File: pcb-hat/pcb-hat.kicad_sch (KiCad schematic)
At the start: 64 parts, among them Q1 NTMFS5C468NLT1G, Q2 Q_NPN, Q3 Q_PMOS_GSD, U1 AOZ6605PI-1, U2 INA219AxD, U3 INA219AxD, U4 HTD Servo, U5 Power_Connector, U6 AOZ6605PI-1, U7 Raspberry_Pi_Generic

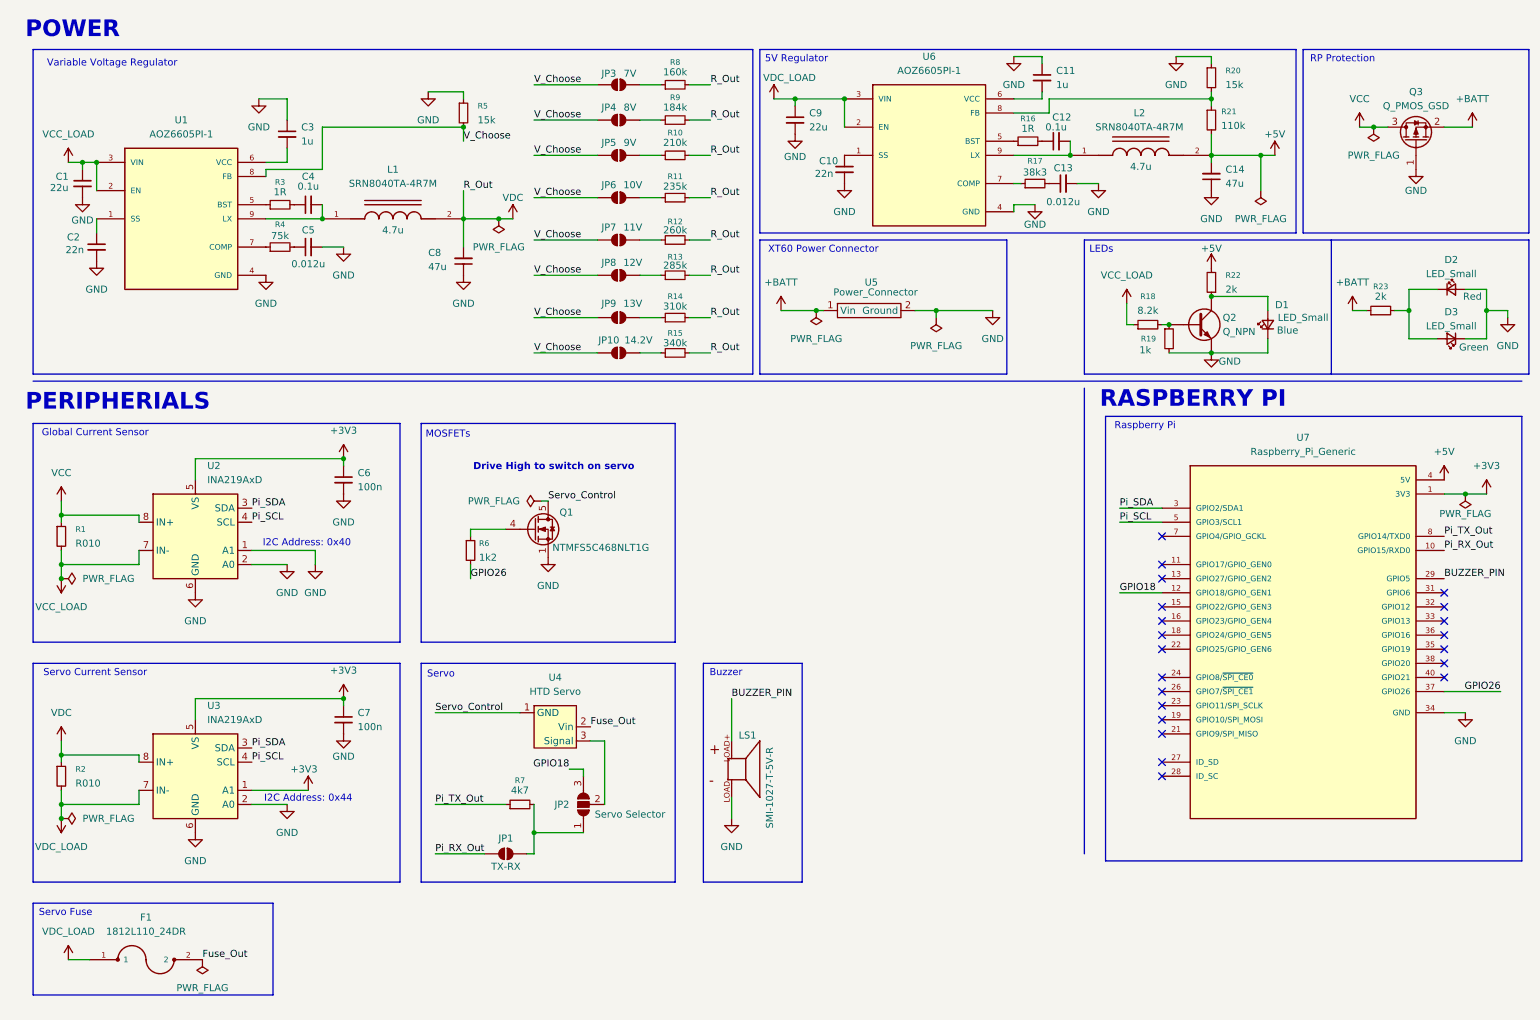
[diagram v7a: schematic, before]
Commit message: Update schematic and reroute PCB
See the github PR for all changes
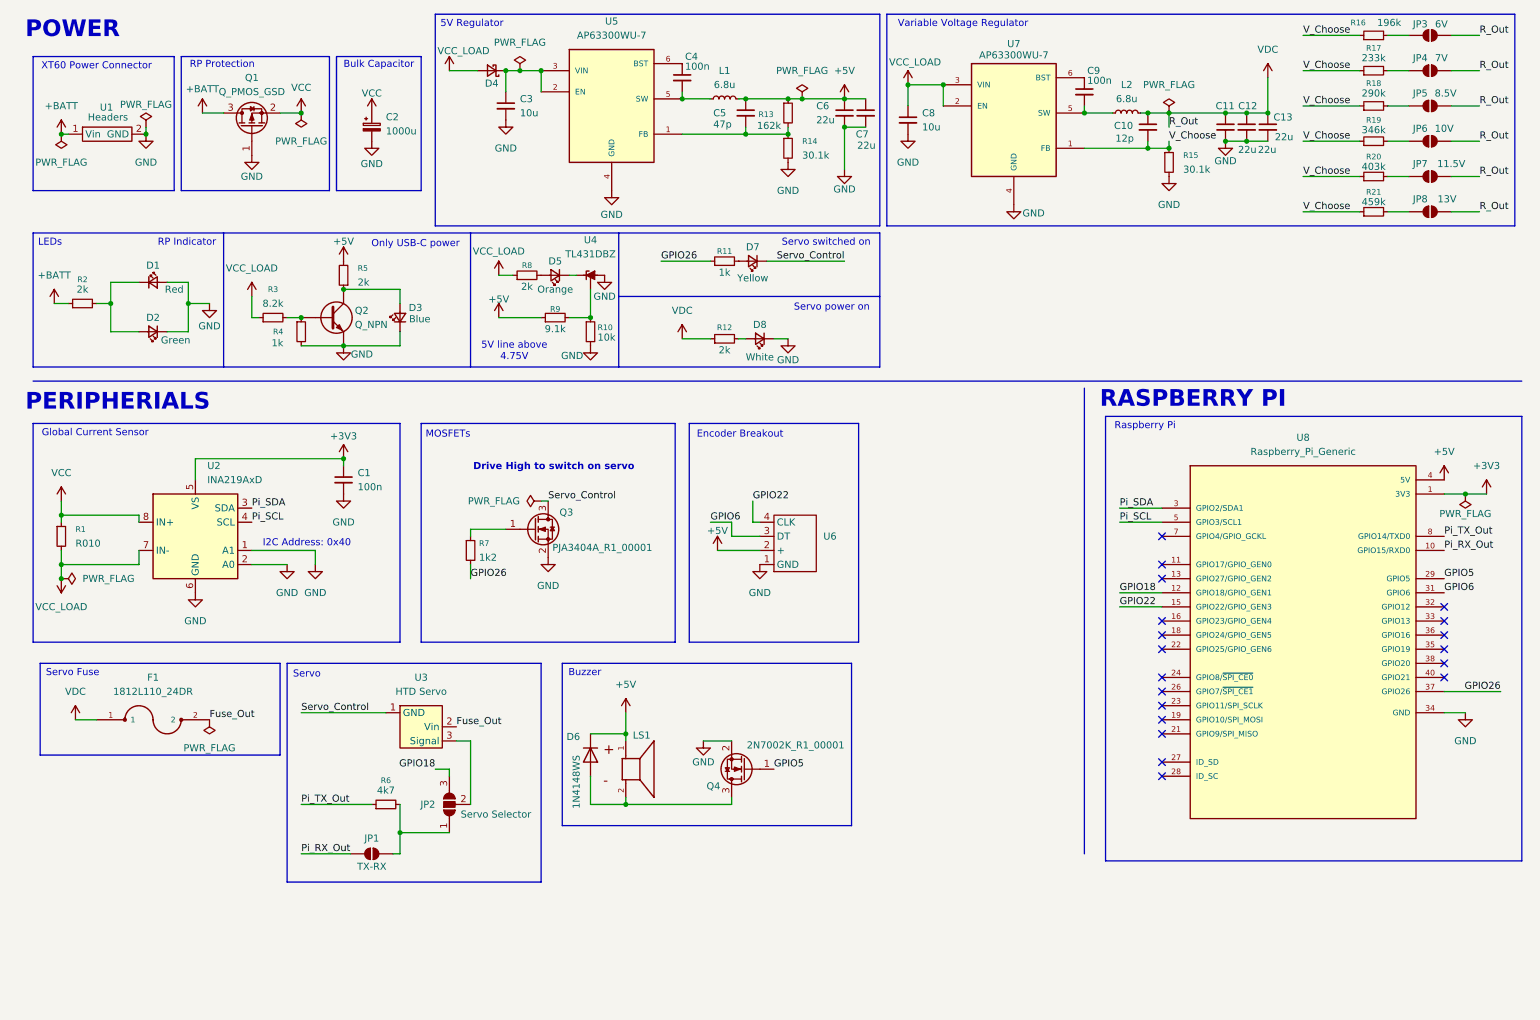
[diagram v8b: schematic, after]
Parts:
- removed C1: 22u, Capacitor_SMD:C_0603_1608Metric_Pad1.08x0.95mm_HandSolder, symbol Device:C_Small
- removed C14: 47u, Capacitor_SMD:C_1206_3216Metric_Pad1.33x1.80mm_HandSolder, symbol Device:C_Small
- removed C2: 22n, Capacitor_SMD:C_0603_1608Metric_Pad1.08x0.95mm_HandSolder, symbol Device:C_Small
- removed JP10, JP9: SolderJumper_2_Open, Jumper:SolderJumper-2_P1.3mm_Open_RoundedPad1.0x1.5mm, symbol Jumper:SolderJumper_2_Open
- removed L1, L2: SRN8040TA-4R7M, pcb_hat:IND_SRN8040TA-4R7M, symbol PiHatComponents:SRN8040TA-4R7M
- removed R16, R3: 1R, Resistor_SMD:R_0603_1608Metric_Pad0.98x0.95mm_HandSolder, symbol Device:R_Small
- removed R17: 38k3, Resistor_SMD:R_0603_1608Metric_Pad0.98x0.95mm_HandSolder, symbol Device:R_Small
- removed R2: R010, Resistor_SMD:R_0603_1608Metric_Pad0.98x0.95mm_HandSolder, symbol Device:R_Small
- removed R20, R5: 15k, Resistor_SMD:R_0603_1608Metric_Pad0.98x0.95mm_HandSolder, symbol Device:R_Small
- removed R21: 110k, Resistor_SMD:R_0603_1608Metric_Pad0.98x0.95mm_HandSolder, symbol Device:R_Small
- removed R4: 75k, Resistor_SMD:R_0603_1608Metric_Pad0.98x0.95mm_HandSolder, symbol Device:R_Small
- removed U1, U6: AOZ6605PI-1, pcb_hat:SOIC127P600X170-9N, symbol PiHatComponents:AOZ6605PI-1
- removed U3: INA219AxD, Package_SO:SOIC-8_3.9x4.9mm_P1.27mm, symbol Sensor_Energy:INA219AxD
- added C2: 1000u, Capacitor_SMD:CP_Elec_10x10.5, symbol Device:C_Polarized_Small
- added C6: 22u, Capacitor_SMD:C_0603_1608Metric_Pad1.08x0.95mm_HandSolder, symbol Device:C_Small
- added D4: SS3P4-M3/84A, Diode_SMD:D_SMP_DO-220AA, symbol Device:D_Schottky_Small
- added D5, D7, D8: LED_Small, LED_SMD:LED_0603_1608Metric_Pad1.05x0.95mm_HandSolder, symbol Device:LED_Small
- added D6: 1N4148WS, Diode_SMD:D_SOD-323, symbol Diode:1N4148WS
- added L1, L2: 6.8u, pcb_hat:IND_ETQP4M6R8KVK, symbol Device:L_Small
- added Q4: 2N7002K_R1_00001, Package_TO_SOT_SMD:TSOT-23, symbol Transistor_FET:Q_NMOS_GSD
- added R10: 10k, Resistor_SMD:R_0603_1608Metric_Pad0.98x0.95mm_HandSolder, symbol Device:R_Small
- added R11: 1k, Resistor_SMD:R_0603_1608Metric_Pad0.98x0.95mm_HandSolder, symbol Device:R_Small
- added R12, R8: 2k, Resistor_SMD:R_0603_1608Metric_Pad0.98x0.95mm_HandSolder, symbol Device:R_Small
- added R13: 162k, Resistor_SMD:R_0603_1608Metric_Pad0.98x0.95mm_HandSolder, symbol Device:R_Small
- added R9: 9.1k, Resistor_SMD:R_0603_1608Metric_Pad0.98x0.95mm_HandSolder, symbol Device:R_Small
- added U4: TL431DBZ, Package_TO_SOT_SMD:SOT-23, symbol Reference_Voltage:TL431DBZ
- added U5, U7: AP63300WU-7, pcb_hat:SOT95P280X100-6N, symbol PiHatComponents:AP63300WU-7
- added U6: ~, Connector_PinHeader_2.54mm:PinHeader_1x04_P2.54mm_Vertical, symbol PiHatComponents:RotaryEncoderPinHeader
- C10: value 22n -> 12p; Digikey PN CGA3E2X7R1H223K080AA -> (none)
- C11: value 1u -> 22u; Digikey PN CL10B105KA8NNNC -> (none)
- C12: value 0.1u -> 22u; Digikey PN C0603C104K3RACTU -> (none)
- C13: value 0.012u -> 22u; Digikey PN CC0603JRX7R8BB123 -> (none)
- C3: value 1u -> 10u; Digikey PN CL10B105KA8NNNC -> (none)
- C4: value 0.1u -> 100n; Digikey PN C0603C104K3RACTU -> (none)
- C5: value 0.012u -> 47p; Digikey PN CC0603JRX7R8BB123 -> (none)
- C7: value 100n -> 22u; Digikey PN C0603C104K3RACTU -> (none)
- C8: value 47u -> 10u; footprint Capacitor_SMD:C_1206_3216Metric_Pad1.33x1.80mm_HandSolder -> Capacitor_SMD:C_0603_1608Metric_Pad1.08x0.95mm_HandSolder; Digikey PN C3216X5R1E476M160AC -> (none)
- C9: value 22u -> 100n; Digikey PN CL10A226MP8NUNE -> (none)
- D1: renamed from D2; footprint pcb_hat:LEDLSQ97601N1Q21 -> LED_SMD:LED_0603_1608Metric_Pad1.05x0.95mm_HandSolder
- D2: renamed from D3; footprint pcb_hat:LEDM1608X80 -> LED_SMD:LED_0603_1608Metric_Pad1.05x0.95mm_HandSolder
- D3: renamed from D1; footprint pcb_hat:LEDC1608X35N -> LED_SMD:LED_0603_1608Metric_Pad1.05x0.95mm_HandSolder
- JP3: V_out 7V -> 6V
- JP4: V_out 8V -> 7V
- JP5: V_out 9V -> 8.5V
- JP7: V_out 11V -> 11.5V
- JP8: V_out 12V -> 13V
- LS1: value SMI-1027-T-5V-R -> ~
- Q2: footprint pcb_hat:MTR_MMBT2222A-TP_MCE -> Package_TO_SOT_SMD:TSOT-23
- Q3: renamed from Q1; value NTMFS5C468NLT1G -> PJA3404A_R1_00001; footprint pcb_hat:NRVTS10100EMFST1G -> Package_TO_SOT_SMD:TSOT-23; symbol PiHatComponents:NMOS_SERVO_CUTOFF -> Transistor_FET:Q_NMOS_GSD; Digikey PN NTMFS5C468NLT1G -> 3757-PJA3404A_R1_00001CT-ND
- R14: value 310k -> 30.1k; Digikey PN CRCW0603309KFKEA -> (none)
- R15: value 340k -> 30.1k; Digikey PN RC0603FR-07340KL -> (none)
- R16: renamed from R8; value 160k -> 196k
- R17: renamed from R9; value 184k -> 233k
- R18: renamed from R10; value 210k -> 290k
- R19: renamed from R11; value 235k -> 346k
- R20: renamed from R12; value 260k -> 403k
- R21: renamed from R13; value 285k -> 459k
- U1: renamed from U5; value Power_Connector -> Headers
- renumbered C6 to C1, Q3 to Q1, R23 to R2, R18 to R3, R19 to R4, R22 to R5, R7 to R6, R6 to R7, U4 to U3, U7 to U8
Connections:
- net +3V3: no longer C7.1
- net +5V: now also C5.1, C7.1, LS1.1, C6.1, D6.1 (K), L1.2, R13.1, R9.1, U6.2 (+)
- net +BATT: now also Q1.3 (D); no longer Q1.2 (S)
- net GND: now also C11.2, C12.2, C3.2, C8.2, R14.2, R15.2, C2.2, C6.2, D8.1 (K), Q4.2 (S), R10.2, U4.3 (A), U5.4 (GND), U6.1 (GND), U7.4 (GND); no longer C10.2, C11.1, C3.1, C5.2, C8.1, C9.2, LS1.LOAD-, Q3.1 (S), Q3.3 (S)
- net GPIO26: now also R11.1
- net Servo_Control: now also Q3.3 (D), D7.1 (K); no longer Q3.5 (D), Q3.6 (D), Q3.7 (D), Q3.8 (D), Q3.9 (D)
- net VCC: now also Q1.2 (S), C2.1; no longer Q1.3 (D)
- net VCC_LOAD: now also C8.1, D4.2 (A), R8.1, U7.2 (EN), U7.3 (VIN)
- net VDC: now also C10.1, C11.1, C12.1, C13.1, F1.1, JP3.2 (B), JP4.2 (B), JP5.2 (B), JP6.2 (B), JP7.2 (B), JP8.2 (B), L2.2, R12.1; no longer C8.2, R14.2, R15.2, R16.2, R17.2, R18.2, R19.2, R20.2, R21.2
- net V_Choose: now also C10.2, R15.1, R16.1, R17.1, R18.1, R19.1, R20.1, R21.1, U7.1 (FB); no longer JP3.1 (A), JP4.1 (A), JP5.1 (A), JP6.1 (A), JP7.1 (A), JP8.1 (A)
- net at C4.1: now also U5.6 (BST)
- net at C4.2: now also L1.1, U5.5 (SW)
- net at R14.1: now also C5.2, R13.2, U5.1 (FB)
- net GPIO22: now reaches U8.15 (GPIO22/GPIO_GEN3)
- net GPIO22: now also U6.4 (CLK)
- net GPIO6: now reaches U8.31 (GPIO6)
- net GPIO6: now also U6.3 (DT)
- net at R7.1: now also Q3.1 (G); no longer Q3.4 (G)
- net BUZZER_PIN renamed GPIO5
- net GPIO5: now also Q4.1 (G); no longer LS1.LOAD+
- net VDC_LOAD: no longer names the net of C9.1
- net VDC_LOAD: now also U7.6 (BST); no longer F1.1
- new net: C3.1, D4.1 (K), U5.2 (EN), U5.3 (VIN)
- new net: C9.2, L2.1, U7.5 (SW)
- new net: JP6.1 (A), R19.2
- new net: D5.1 (K), U4.1 (K)
- new net: R10.1, R9.2, U4.2 (REF)
- new net: D8.2 (A), R12.2
- new net: D7.2 (A), R11.2
- new net: JP5.1 (A), R18.2
- new net: JP3.1 (A), R16.2
- new net: D6.2 (A), LS1.2, Q4.3 (D)
- new net: JP7.1 (A), R20.2
- new net: JP8.1 (A), R21.2
- new net: D5.2 (A), R8.2
- new net: JP4.1 (A), R17.2
- no-connect marks 21 -> 19
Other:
- note added: "5V line above 4.75V"
- note added: "Bulk Capacitor"
- note added: "Encoder Breakout"
- note added: "Only USB-C power"
- note added: "RP Indicator"
- note added: "Servo power on"
- note added: "Servo switched on"
- note removed: "I2C Address: 0x44"
- note removed: "Servo Current Sensor"
- moved on the sheet: D1, D2, D3, F1, JP1, JP2, JP3, JP4, JP5, JP6, JP7, JP8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
